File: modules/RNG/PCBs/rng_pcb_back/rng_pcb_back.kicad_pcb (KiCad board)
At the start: 2 copper layers, 50 x 100 mm, 31 parts, among them J10 Conn_01x08_Socket, J11 Eurorack_2x8_Power, J7 Conn_01x07_Socket, J8 Conn_02x03_Socket, J9 Conn_01x06_Socket, U1 TLC5940NT, U2 MCP4922, U3 MCP6004, U4 TL072, U5 LM4040BCZ-5

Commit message: added async analog reading to RNG
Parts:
- R17: value 100kΩ -> 15kΩ
- renumbered REF** to G1
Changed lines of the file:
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@@
         (effects (font (size 1 1) (thickness 0.15)))
     )
-    (fp_text value "100kΩ" (at 3.81 2.37) (layer "F.Fab")
+    (fp_text value "15kΩ" (at 3.81 2.37) (layer "F.Fab")
         (effects (font (size 1 1) (thickness 0.15)))
     )
@@
   (footprint "FreeModualr:logo_small" (layer "F.Cu")
     (at 34.602337 56.615091)
-    (fp_text reference "REF**" (at 0 -0.5 unlocked) (layer "F.SilkS") hide
+    (fp_text reference "G1" (at 0 -0.5 unlocked) (layer "F.SilkS") hide
         (effects (font (size 1 1) (thickness 0.1)))
     )

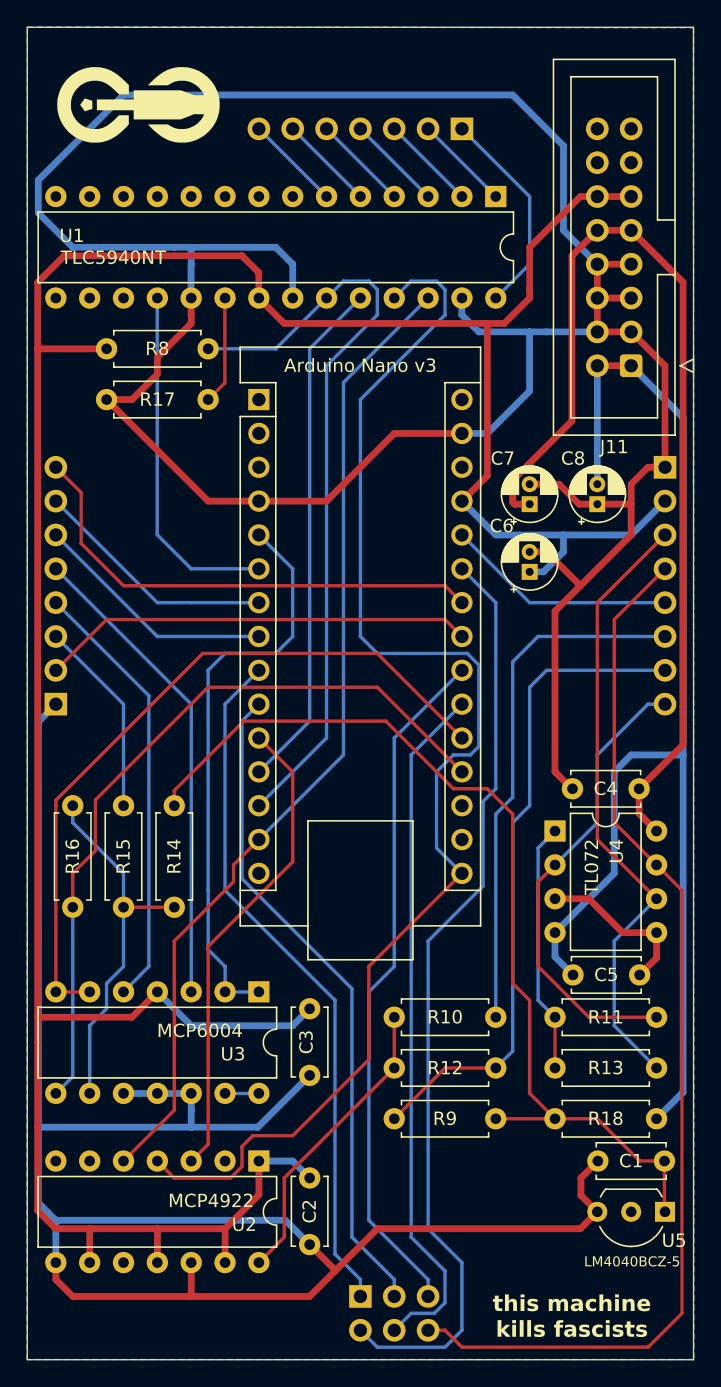
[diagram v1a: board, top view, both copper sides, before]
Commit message: fix -5v ref in rng pcb
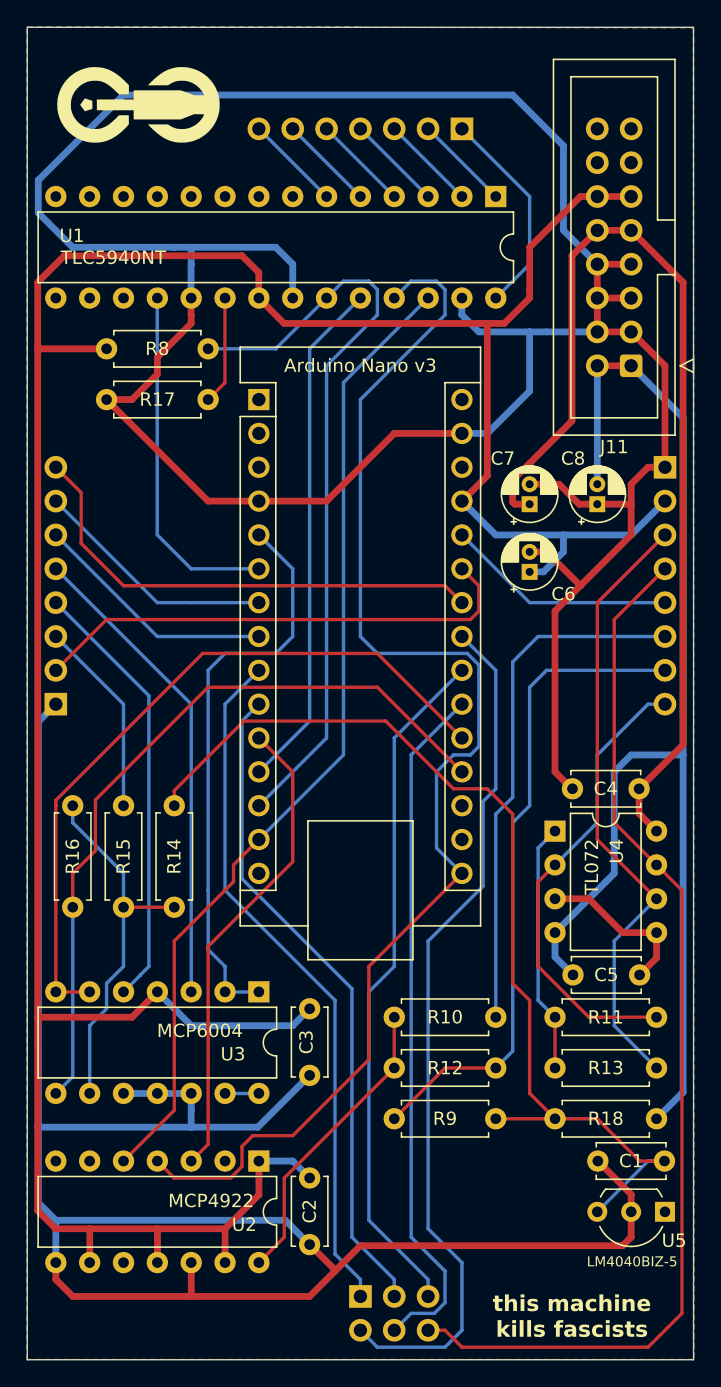
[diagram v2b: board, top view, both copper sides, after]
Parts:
- R16: value 100kΩ -> 50kΩ
- R18: value 470Ω -> 15kΩ
- U5: value LM4040BCZ-5 -> LM4040BIZ-5
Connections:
- A1 pad 23: POT_BIAS -> TRIG_SWTICH
- A1 pad 25: TRIG_SWTICH -> POT_BIAS
- U5 pad 1: VREF_-5 -> (no net)
- U5 pad 2: (no net) -> GND
- U5 pad 3: GND -> VREF_-5
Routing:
- net TRIG_SWTICH: track 70.0 -> 65.0 mm
- net POT_BIAS: track 32.6 -> 37.3 mm
- net GND: track 375.0 -> 378.7 mm
- net VREF_-5: track 73.6 -> 76.4 mm
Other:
- board text added: "FreeModular RNG back v3.1"
- board text removed: "FreeModular RNG back v3.0"

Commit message: add missing output resistor
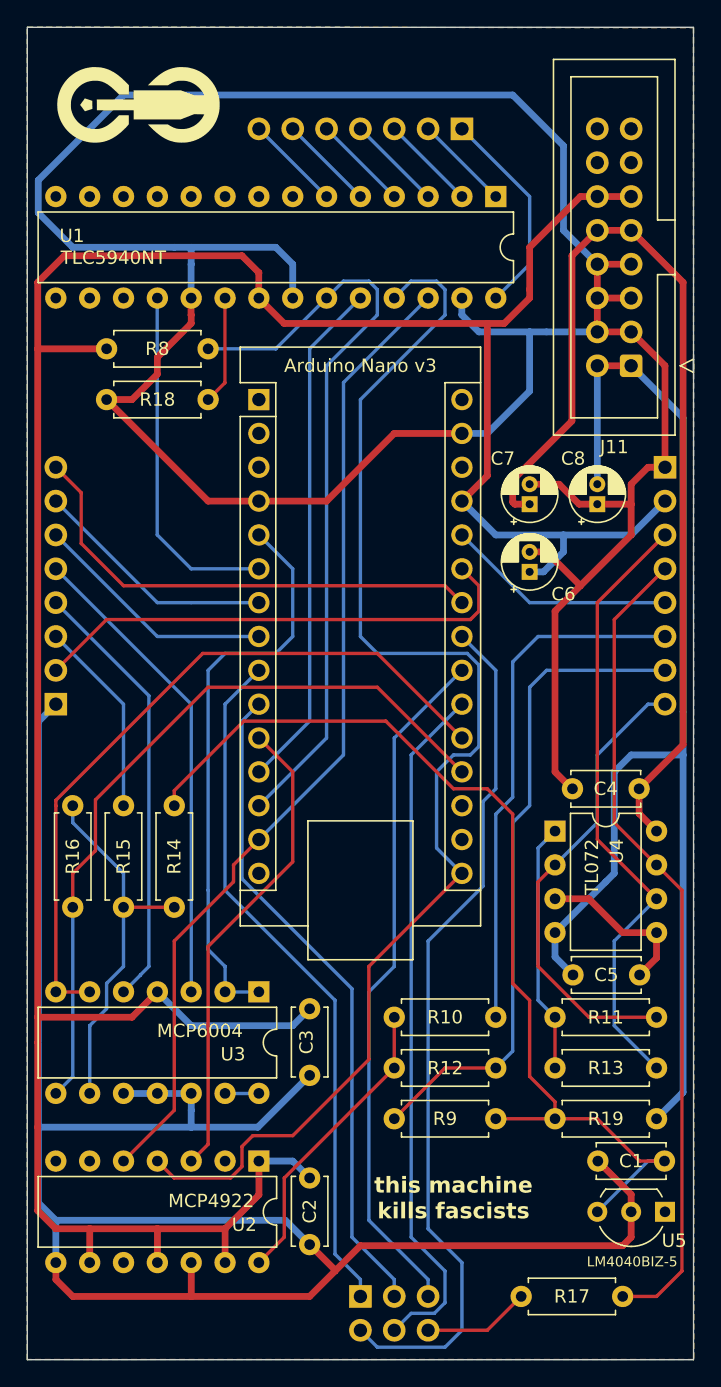
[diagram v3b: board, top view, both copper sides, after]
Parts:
- added R17: 1kΩ, Resistor_THT:R_Axial_DIN0207_L6.3mm_D2.5mm_P7.62mm_Horizontal, F.Cu at (70.5, 146.1)
- renumbered R17 to R18, R18 to R19
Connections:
- J8 pad 6: GAIN_B -> RANDOM_OUT
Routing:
- net GAIN_B: track 80.8 -> 61.6 mm
- net RANDOM_OUT: track 0.00 -> 8.04 mm
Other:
- board text added: "FreeModular RNG back v3.2"
- board text removed: "FreeModular RNG back v3.1"

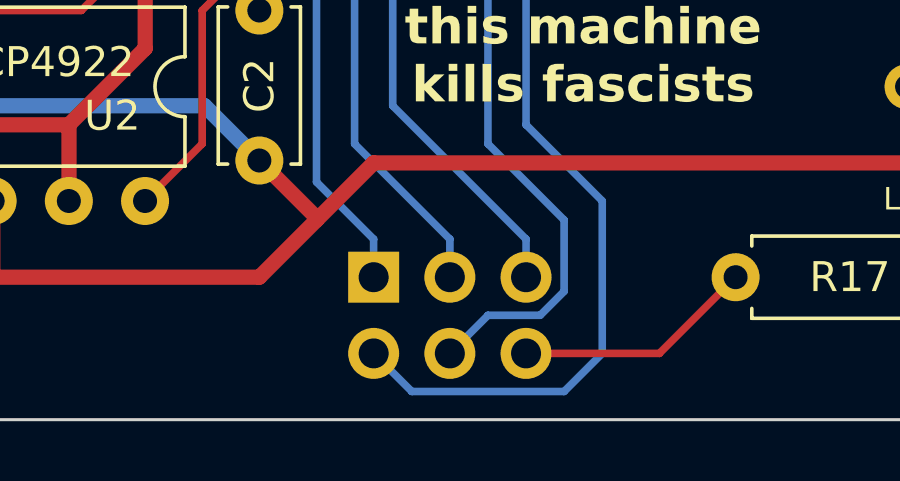
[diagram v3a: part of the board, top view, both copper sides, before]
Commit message: flip silkscreen for pin header
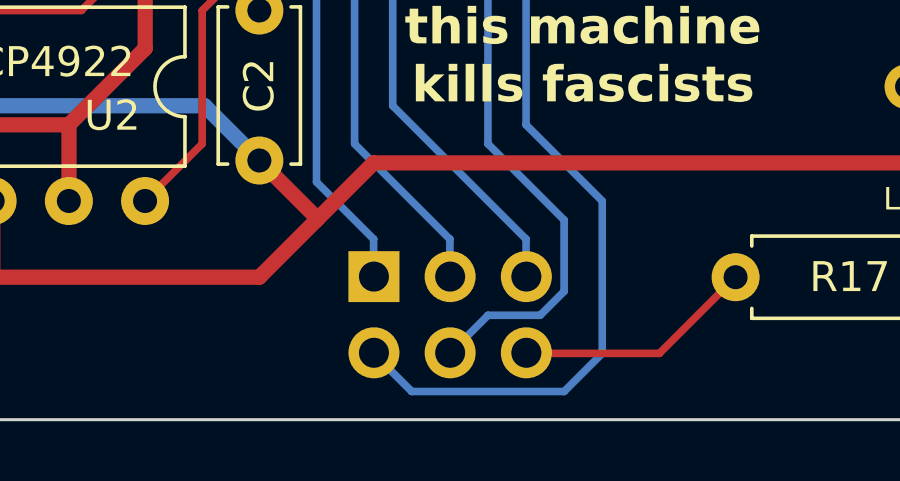
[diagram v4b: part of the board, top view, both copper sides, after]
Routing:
- net GATE_A_OUT: track 50.4 -> 49.7 mm
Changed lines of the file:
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@@
 	(footprint "Connector_PinHeader_2.54mm:PinHeader_2x03_P2.54mm_Vertical"
 		(layer "B.Cu")
-		(at 50.8 146.05 -90)
+		(at 50.81 146.03 -90)
 		(descr "Through hole straight pin header, 2x03, 2.54mm pitch, double rows")
 		(tags "Through hole pin header THT 2x03 2.54mm double row")
@@
 			)
 		)
-		(property "Footprint" ""
-			(at 0 0 -90)
+		(property "Footprint" "Connector_PinHeader_2.54mm:PinHeader_2x03_P2.54mm_Vertical"
+			(at 0 0 90)
 			(unlocked yes)
-			(layer "F.Fab")
+			(layer "B.Fab")
 			(hide yes)
 			(effects
@@
 					(size 1.27 1.27)
 				)
+				(justify mirror)
 			)
 		)
 		(property "Datasheet" ""
-			(at 0 0 -90)
+			(at 0 0 90)
 			(unlocked yes)
-			(layer "F.Fab")
+			(layer "B.Fab")
 			(hide yes)
 			(effects
@@
 					(size 1.27 1.27)
 				)
+				(justify mirror)
 			)
 		)
 		(property "Description" ""
-			(at 0 0 -90)
+			(at 0 0 90)
 			(unlocked yes)
-			(layer "F.Fab")
+			(layer "B.Fab")
 			(hide yes)
 			(effects
@@
 					(size 1.27 1.27)
 				)
+				(justify mirror)
 			)
 		)
@@
 		(fp_line
 			(start -1.33 1.33)
-			(end 0 1.33)
+			(end -1.33 0)
 			(stroke
 				(width 0.12)
@@
 		)
 		(fp_line
+			(start 0 1.33)
+			(end -1.33 1.33)
+			(stroke
+				(width 0.12)
+				(type solid)
+			)
+			(layer "B.SilkS")
+		)
+		(fp_line
 			(start 1.27 1.33)
+			(end 1.27 -1.27)
+			(stroke
+				(width 0.12)
+				(type solid)
+			)
+			(layer "B.SilkS")
+		)
+		(fp_line
+			(start 3.87 1.33)
+			(end 1.27 1.33)
+			(stroke
+				(width 0.12)
+				(type solid)
+			)
+			(layer "B.SilkS")
+		)
+		(fp_line
+			(start 1.27 -1.27)
+			(end -1.33 -1.27)
+			(stroke
+				(width 0.12)
+				(type solid)
+			)
+			(layer "B.SilkS")
+		)
+		(fp_line
+			(start -1.33 -6.41)
+			(end -1.33 -1.27)
+			(stroke
+				(width 0.12)
+				(type solid)
+			)
+			(layer "B.SilkS")
+		)
+		(fp_line
+			(start 3.87 -6.41)
 			(end 3.87 1.33)
 			(stroke
@@
 		)
 		(fp_line
-			(start 3.87 1.33)
-			(end 3.87 -6.41)
+			(start 3.87 -6.41)
+			(end -1.33 -6.41)
 			(stroke
 				(width 0.12)
@@
 		)
 		(fp_line
-			(start -1.33 0)
-			(end -1.33 1.33)
-			(stroke
-				(width 0.12)
-				(type solid)
-			)
-			(layer "B.SilkS")
-		)
-		(fp_line
-			(start -1.33 -1.27)
-			(end 1.27 -1.27)
-			(stroke
-				(width 0.12)
-				(type solid)
-			)
-			(layer "B.SilkS")
-		)
-		(fp_line
-			(start -1.33 -1.27)
-			(end -1.33 -6.41)
-			(stroke
-				(width 0.12)
-				(type solid)
-			)
-			(layer "B.SilkS")
-		)
-		(fp_line
-			(start 1.27 -1.27)
-			(end 1.27 1.33)
-			(stroke
-				(width 0.12)
-				(type solid)
-			)
-			(layer "B.SilkS")
-		)
-		(fp_line
-			(start -1.33 -6.41)
-			(end 3.87 -6.41)
-			(stroke
-				(width 0.12)
-				(type solid)
-			)
-			(layer "B.SilkS")
-		)
-		(fp_line
 			(start -1.8 1.8)
+			(end 4.35 1.8)
+			(stroke
+				(width 0.05)
+				(type solid)
+			)
+			(layer "B.CrtYd")
+		)
+		(fp_line
+			(start 4.35 1.8)
+			(end 4.35 -6.85)
+			(stroke
+				(width 0.05)
+				(type solid)
+			)
+			(layer "B.CrtYd")
+		)
+		(fp_line
+			(start -1.8 -6.85)
+			(end -1.8 1.8)
+			(stroke
+				(width 0.05)
+				(type solid)
+			)
+			(layer "B.CrtYd")
+		)
+		(fp_line
+			(start 4.35 -6.85)
 			(end -1.8 -6.85)
 			(stroke
@@
 		)
 		(fp_line
-			(start 4.35 1.8)
-			(end -1.8 1.8)
-			(stroke
-				(width 0.05)
-				(type solid)
-			)
-			(layer "B.CrtYd")
-		)
-		(fp_line
-			(start -1.8 -6.85)
-			(end 4.35 -6.85)
-			(stroke
-				(width 0.05)
-				(type solid)
-			)
-			(layer "B.CrtYd")
-		)
-		(fp_line
-			(start 4.35 -6.85)
-			(end 4.35 1.8)
-			(stroke
-				(width 0.05)
-				(type solid)
-			)
-			(layer "B.CrtYd")
-		)
-		(fp_line
 			(start 0 1.27)
+			(end -1.27 0)
+			(stroke
+				(width 0.1)
+				(type solid)
+			)
+			(layer "B.Fab")
+		)
+		(fp_line
+			(start 3.81 1.27)
+			(end 0 1.27)
+			(stroke
+				(width 0.1)
+				(type solid)
+			)
+			(layer "B.Fab")
+		)
+		(fp_line
+			(start -1.27 0)
+			(end -1.27 -6.35)
+			(stroke
+				(width 0.1)
+				(type solid)
+			)
+			(layer "B.Fab")
+		)
+		(fp_line
+			(start -1.27 -6.35)
+			(end 3.81 -6.35)
+			(stroke
+				(width 0.1)
+				(type solid)
+			)
+			(layer "B.Fab")
+		)
+		(fp_line
+			(start 3.81 -6.35)
 			(end 3.81 1.27)
-			(stroke
-				(width 0.1)
-				(type solid)
-			)
-			(layer "B.Fab")
-		)
-		(fp_line
-			(start 3.81 1.27)
-			(end 3.81 -6.35)
-			(stroke
-				(width 0.1)
-				(type solid)
-			)
-			(layer "B.Fab")
-		)
-		(fp_line
-			(start -1.27 0)
-			(end 0 1.27)
-			(stroke
-				(width 0.1)
-				(type solid)
-			)
-			(layer "B.Fab")
-		)
-		(fp_line
-			(start -1.27 -6.35)
-			(end -1.27 0)
-			(stroke
-				(width 0.1)
-				(type solid)
-			)
-			(layer "B.Fab")
-		)
-		(fp_line
-			(start 3.81 -6.35)
-			(end -1.27 -6.35)
 			(stroke
 				(width 0.1)
@@
 			(pintype "passive")
 		)
-		(model "${KICAD6_3DMODEL_DIR}/Connector_PinHeader_2.54mm.3dshapes/PinHeader_2x03_P2.54mm_Vertical.wrl"
+		(model "${KICAD8_3DMODEL_DIR}/Connector_PinHeader_2.54mm.3dshapes/PinHeader_2x03_P2.54mm_Vertical.wrl"
 			(offset
 				(xyz 0 0 0)
@@
 		(width 0.254)
 		(layer "B.Cu")
-		(net 10)
-	)
-	(segment
-		(start 53.34 146.05)
-		(end 54.05842 146.05)
-		(width 0.254)
-		(layer "B.Cu")

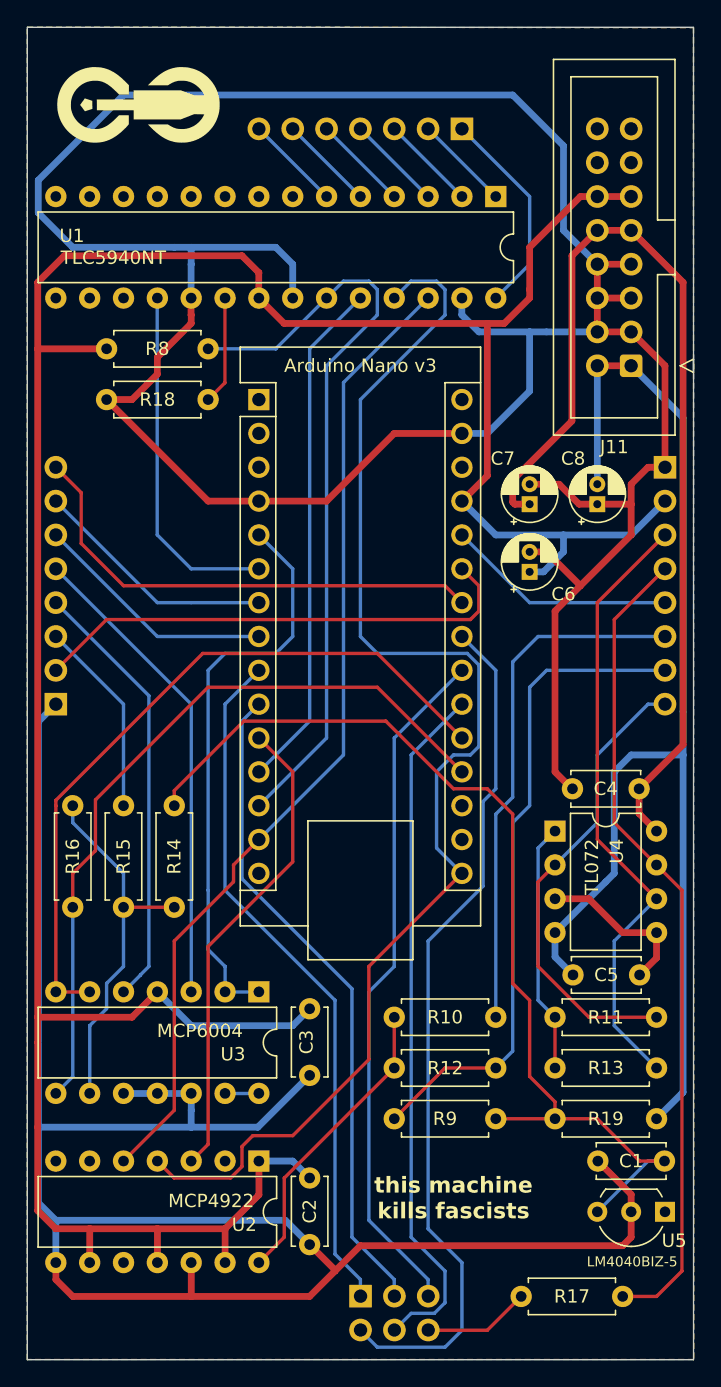
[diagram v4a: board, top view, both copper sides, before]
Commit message: Add SMD option for LED driver on RNG
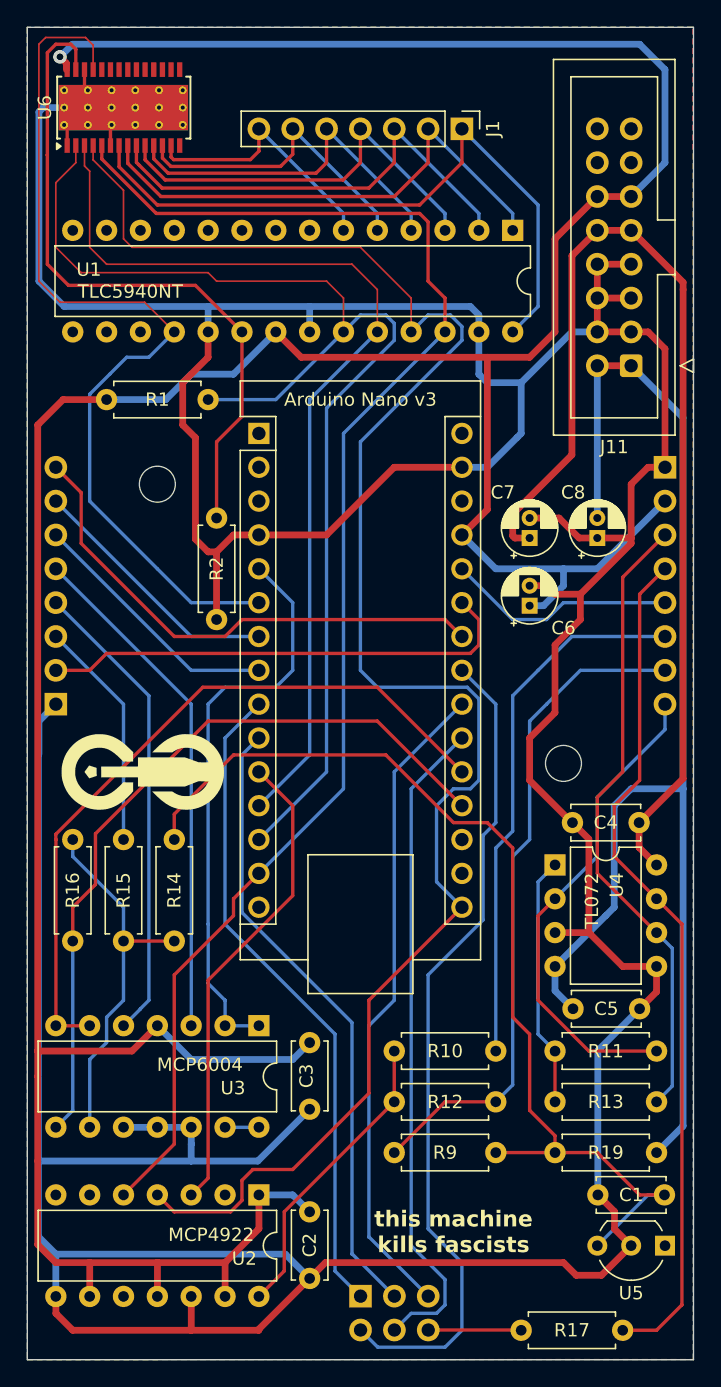
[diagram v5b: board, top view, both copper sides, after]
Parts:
- removed J7: Conn_01x07_Socket, Connector_PinHeader_2.54mm:PinHeader_1x07_P2.54mm_Vertical
- removed R18: 15kΩ, Resistor_THT:R_Axial_DIN0207_L6.3mm_D2.5mm_P7.62mm_Horizontal
- removed R8: 100kΩ, Resistor_THT:R_Axial_DIN0207_L6.3mm_D2.5mm_P7.62mm_Horizontal
- added H1: M2.5, MountingHole:MountingHole_2.7mm_M2.5, F.Cu at (35.6, 85.1)
- added H2: M2.5, MountingHole:MountingHole_2.7mm_M2.5, F.Cu at (66.0, 106.0)
- added J1: Conn_01x07_Socket, Connector_PinHeader_2.54mm:PinHeader_1x07_P2.54mm_Vertical, F.Cu at (58.4, 58.4)
- added R1: 100kΩ, Resistor_THT:R_Axial_DIN0207_L6.3mm_D2.5mm_P7.62mm_Horizontal, F.Cu at (39.4, 78.7)
- added R2: 15kΩ, Resistor_THT:R_Axial_DIN0207_L6.3mm_D2.5mm_P7.62mm_Horizontal, F.Cu at (40.0, 87.6)
- added U6: TLC5940PWP, Package_SO:HTSSOP-28-1EP_4.4x9.7mm_P0.65mm_EP3.4x9.5mm_Mask2.4x6.17mm_ThermalVias, F.Cu at (33.0, 56.8)
- G1: footprint FreeModualr:logo_small -> FreeModular:logo_small
- U5: footprint Package_TO_SOT_THT:TO-92L_Inline_Wide -> Package_TO_SOT_THT:TO-92_Inline_Wide
- moved G1 50.1 mm to (34.9, 106.7)
- moved U1 2.84 mm to (62.2, 66.0)
- moved C1 2.54 mm to (73.6, 138.4)
- moved U2 2.54 mm to (43.2, 138.4)
- moved U5 2.54 mm to (73.7, 142.2)
- moved A1 2.54 mm to (43.2, 81.3)
- moved C3 2.54 mm to (47.0, 127.0)
- moved R10 2.54 mm to (53.3, 127.6)
- moved R11 2.54 mm to (73.0, 127.6)
- moved R14 2.54 mm to (36.8, 111.8)
- moved R15 2.54 mm to (33.0, 111.8)
- moved R16 2.54 mm to (29.2, 111.8)
- moved U3 2.54 mm to (43.2, 125.7)
- moved U4 2.54 mm to (65.4, 113.7)
- moved C2 2.54 mm to (47.0, 139.7)
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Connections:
- U1 pad 1: Net-(J7-Pin_2) -> /Led Driver/LED_2
- U1 pad 2: Net-(J7-Pin_3) -> /Led Driver/LED_3
- U1 pad 20: Net-(U1-IREF) -> /Led Driver/IREF
- U1 pad 28: Net-(J7-Pin_1) -> /Led Driver/LED_1
- U1 pad 3: Net-(J7-Pin_4) -> /Led Driver/LED_4
- U1 pad 4: Net-(J7-Pin_5) -> /Led Driver/LED_5
- U1 pad 5: Net-(J7-Pin_6) -> /Led Driver/LED_6
- U1 pad 6: Net-(J7-Pin_7) -> /Led Driver/LED_7
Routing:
- net /Led Driver/IREF: track 0.00 -> 51.4 mm
- net /Led Driver/LED_1: track 0.00 -> 50.8 mm
- net +5V: track 221.4 -> 269.6 mm, vias 0 -> 1
- net LED_PWM_REF: track 26.5 -> 68.0 mm
- net /Led Driver/LED_2: track 0.00 -> 38.7 mm
- net SPI_MOSI: track 74.2 -> 111.0 mm
- net LED_BLANK: track 57.5 -> 93.8 mm
- net /Led Driver/LED_3: track 0.00 -> 35.1 mm
- net LED_LATCH: track 38.7 -> 73.1 mm
- net SPI_SCK: track 99.4 -> 133.7 mm
- net /Led Driver/LED_4: track 0.00 -> 31.2 mm
- net /Led Driver/LED_5: track 0.00 -> 27.5 mm
- net /Led Driver/LED_6: track 0.00 -> 23.5 mm
- net /Led Driver/LED_7: track 0.00 -> 19.7 mm
- net Net-(J7-Pin_1): track 15.9 -> 0.00 mm
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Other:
- board text added: "FreeModular RNG back v3.3"
- board text removed: "FreeModular RNG back v3.2"
